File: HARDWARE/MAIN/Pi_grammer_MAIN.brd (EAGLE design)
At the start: 73.7 x 78.7 mm, 56 parts, among them J3 TARGET_copy, Q1 220mA/50V/3.5Ω, Q2 220mA/50V/3.5Ω, Q3 220mA/50V/3.5Ω, Q4 220mA/50V/3.5Ω, Q5 220mA/50V/3.5Ω, U1 AT42QT1010UDFN, U2 74LVC4066

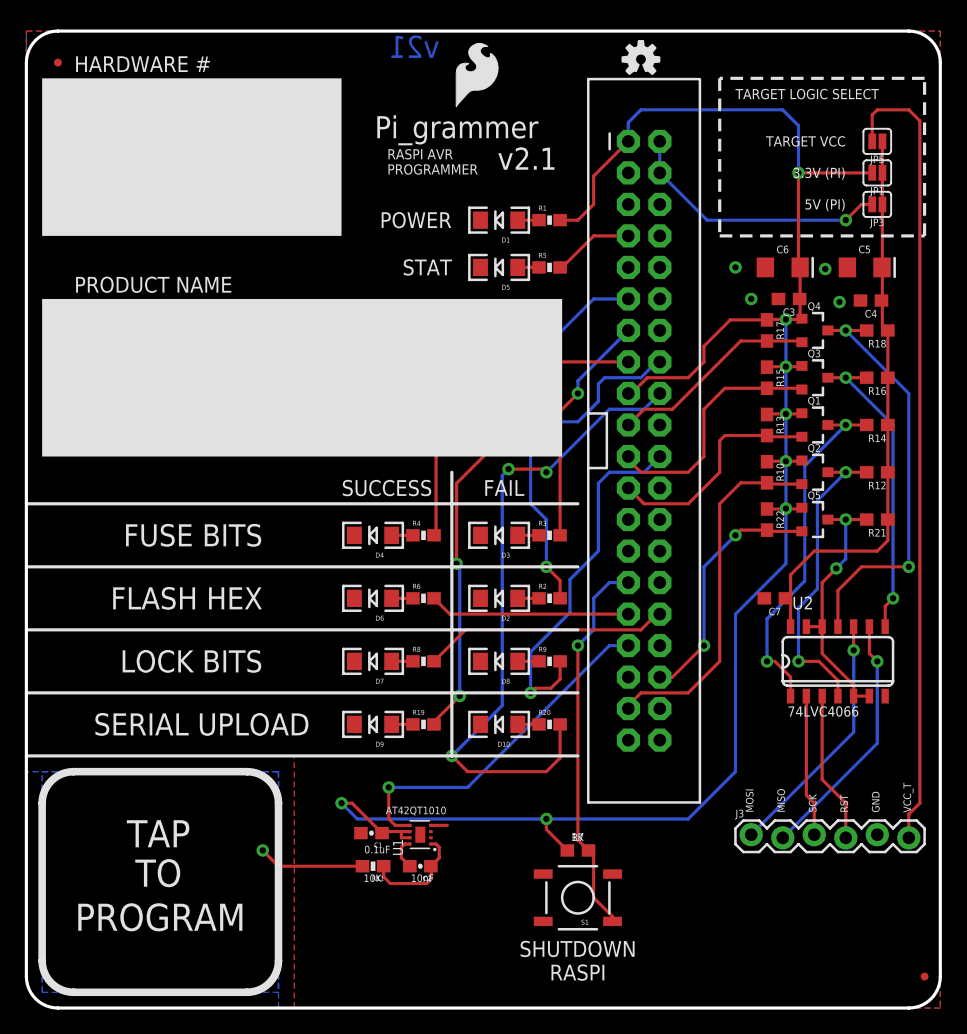
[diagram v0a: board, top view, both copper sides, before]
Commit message: pi_grammer_MAIN updates for storefront product
-moved to RA SMT 1x6 header for programming lines to cable, had to re-route a few things, MISO and MOSI have a much better direct route now.
-Enlarged most silk to standard 0.05
-changed text silk on "blank boxes" to more generic use case terms - project name, version, date etc.
-added prod ID to switch IC
-updated copper and sch version number to v22
-added large sparkfun logo to bottom side silk
-removed passive component values silk - this is only used during QC testing hardware assembly (when we build them by hand)
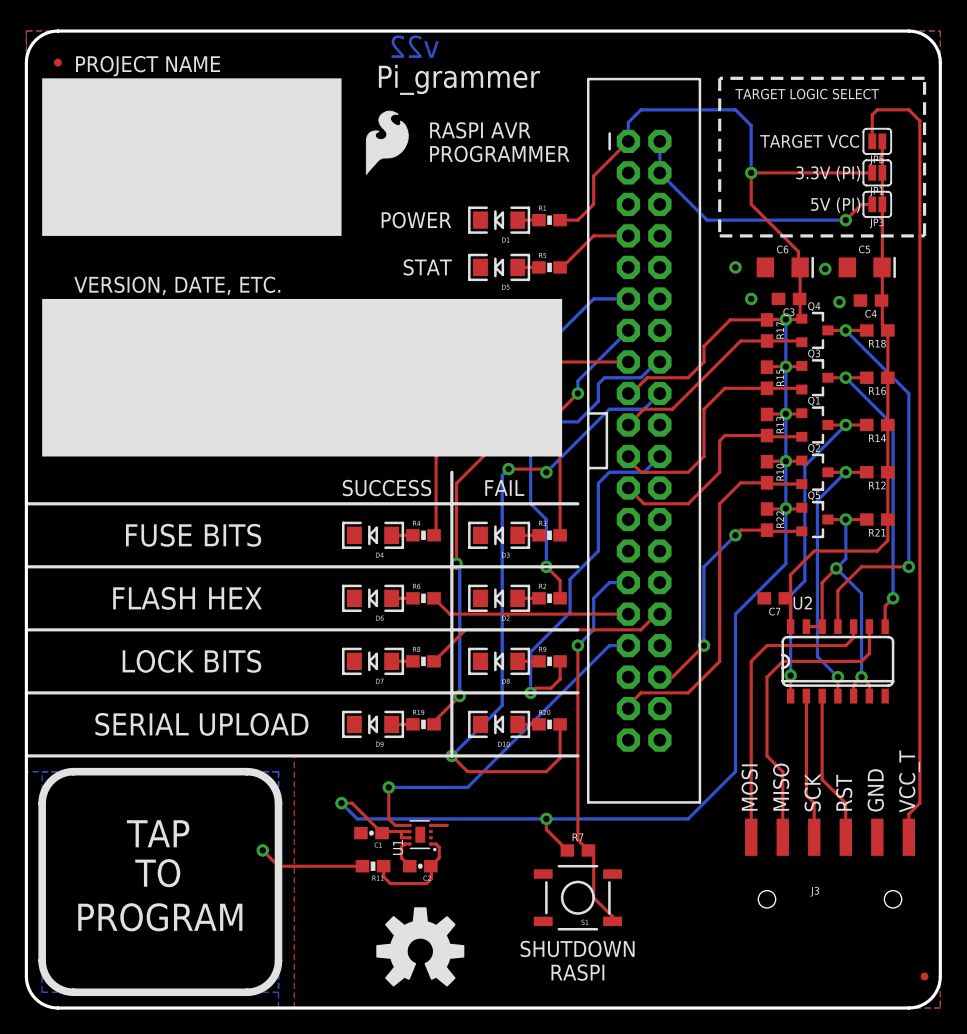
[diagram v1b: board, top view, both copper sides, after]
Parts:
- added LOGO3: SFE_LOGO_NAME.6_INCH, SparkFun-Aesthetics:SFE_LOGO_NAME_.6
- J3: value TARGET_copy -> RA 6Pin SMD; device SparkFun-Connectors:1X06_LOCK -> SparkFun-Connectors:1X06-SMD_RA_MALE
- LOGO2: value OSHW-LOGOS -> OSHW-LOGOL; device SparkFun-Aesthetics:OSHW-LOGO-S -> SparkFun-Aesthetics:OSHW-LOGO-L
- moved LOGO2 74.0 mm to (31.8, 4.57)
- moved LOGO1 9.07 mm to (27.1, 66.9)
- moved J3 8.21 mm to (64.8, 8.76)
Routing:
- net PGM_CTRL_T: track 21.7 -> 27.0 mm, vias 2 -> 3
- net BRD_MISO: track 20.4 -> 24.6 mm, vias 1 -> 0
- net BRD_MOSI: track 20.2 -> 24.1 mm, vias 1 -> 0
- net RST_T: track 25.0 -> 22.8 mm
- net SCK_T: track 28.8 -> 26.8 mm
- net 3.3V: track 159.1 -> 160.7 mm
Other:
- board text added: "PROJECT NAME"
- board text added: "VERSION, DATE, ETC."
- board text added: "v22"
- board text removed: "0.1uF"
- board text removed: "10K"
- board text removed: "10nF"
- board text removed: "1K"
- board text removed: "AT42QT1010"
- board text removed: "HARDWARE #"
- board text removed: "PRODUCT NAME"
- board text removed: "v2.1"
- board text removed: "v21"

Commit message: updated AT42QT1010 to pull from the proper sparkfun eagle sensor library dev
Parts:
- U1: value AT42QT1010UDFN -> AT42QT1010 - UDFN; device Testing:UDFN/USON_8_PAD -> SparkFun-Sensors:UDFN/USON_8_PAD
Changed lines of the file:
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@@
 </element>
 <element name="LOGO2" library="SparkFun-Aesthetics" package="OSHW-LOGO-L" value="OSHW-LOGOL" x="31.75" y="4.572"/>
-<element name="U1" library="Testing" package="UDFN/USON_8_PAD" value="AT42QT1010UDFN" x="31.75" y="13.97" rot="R90">
+<element name="U1" library="SparkFun-Sensors" package="UDFN/USON_8_PAD" value="AT42QT1010 - UDFN" x="31.75" y="13.97" rot="R90">
 <attribute name="PROD_ID" value="IC-11778" x="31.75" y="13.97" size="1.778" layer="27" rot="R90" display="off"/>
+<attribute name="VALUE" value="AT42QT1010 - UDFN" x="31.75" y="13.97" size="1.778" layer="27" rot="R90" display="off"/>
 </element>
 <element name="C1" library="SparkFun-Capacitors" package="0603-CAP" value="0.1uF" x="27.813" y="14.097" rot="R180">

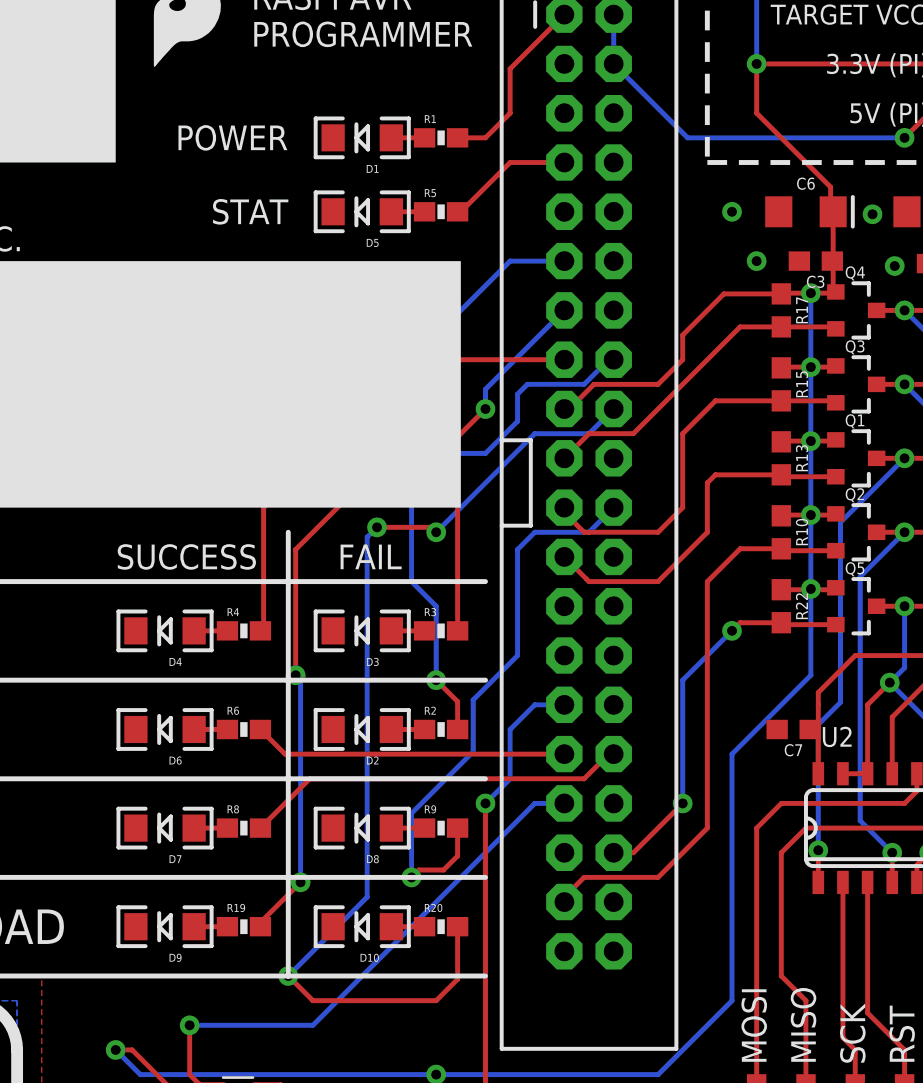
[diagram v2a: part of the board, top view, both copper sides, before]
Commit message: updated switch (U2) to use sparkfun eagle library
also updated all libraries and the LEDs silk changed to updated versions of 1206 packages
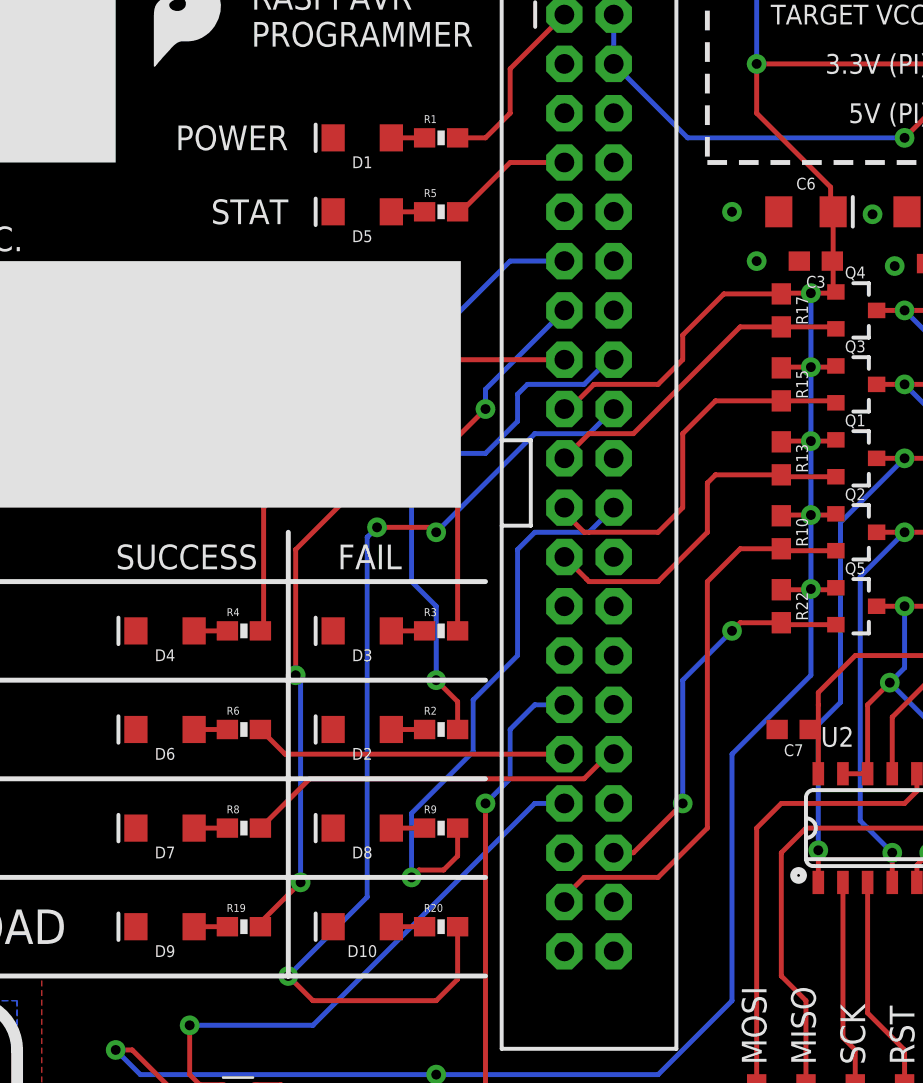
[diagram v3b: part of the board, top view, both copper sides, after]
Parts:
- U2: device Testing:SO14 -> SparkFun-IC-Logic:SO14
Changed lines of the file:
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@@
 <attribute name="PROD_ID" value="CAP-00810" x="60.325" y="21.59" size="1.778" layer="27" font="vector" ratio="15" rot="R180" display="off"/>
 </element>
-<element name="U2" library="Testing" package="SO14" value="74LVC4066" x="64.77" y="27.94" smashed="yes">
+<element name="U2" library="SparkFun-IC-Logic" package="SO14" value="74LVC4066" x="64.77" y="27.94" smashed="yes">
 <attribute name="NAME" x="61.722" y="32.131" size="1.016" layer="25" font="vector" ratio="10"/>
 <attribute name="PROD_ID" value="IC-13944" x="64.77" y="27.94" size="1.778" layer="27" display="off"/>

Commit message: schematic frame update to CC 4.0
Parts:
- added FRAME1: FRAME-LETTER, SparkFun-Aesthetics:CREATIVE_COMMONS
- FD1, FD2: device SparkFun-Aesthetics:MICRO-FIDUCIAL -> SparkFun-Aesthetics:FIDUCIAL-MICRO
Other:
- board text added: "Pete Lewis"

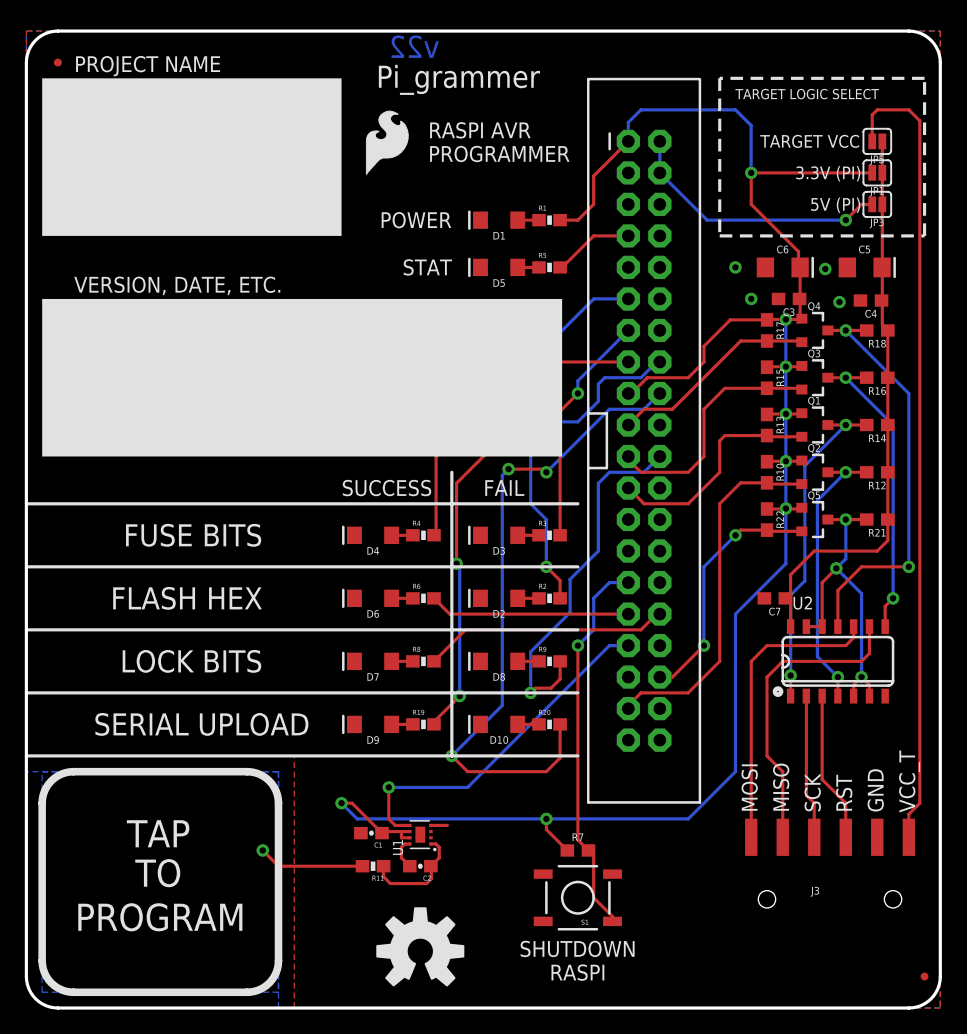
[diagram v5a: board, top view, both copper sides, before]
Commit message: schematic cleanup and notes
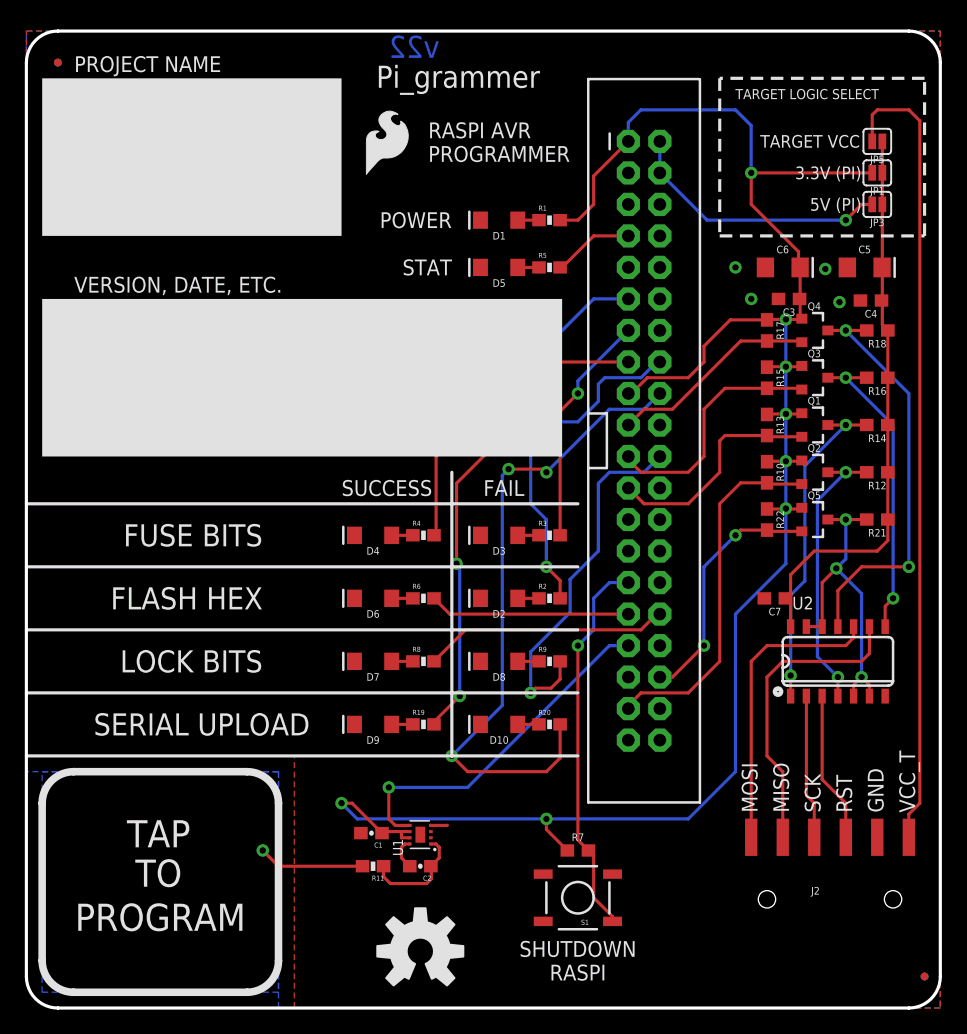
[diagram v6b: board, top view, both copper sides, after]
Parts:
- added FD3, FD4: FIDUCIALUFIDUCIAL, SparkFun-Aesthetics:FIDUCIAL-MICRO
- J2: value RA 6Pin SMD -> SPI
- JP5: value JUMPER-SMT_2_NC_PASTE_SILK -> (none)
- renumbered J3 to J2, JP2 to J1
